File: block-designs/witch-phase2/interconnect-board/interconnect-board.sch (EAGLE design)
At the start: 10 parts

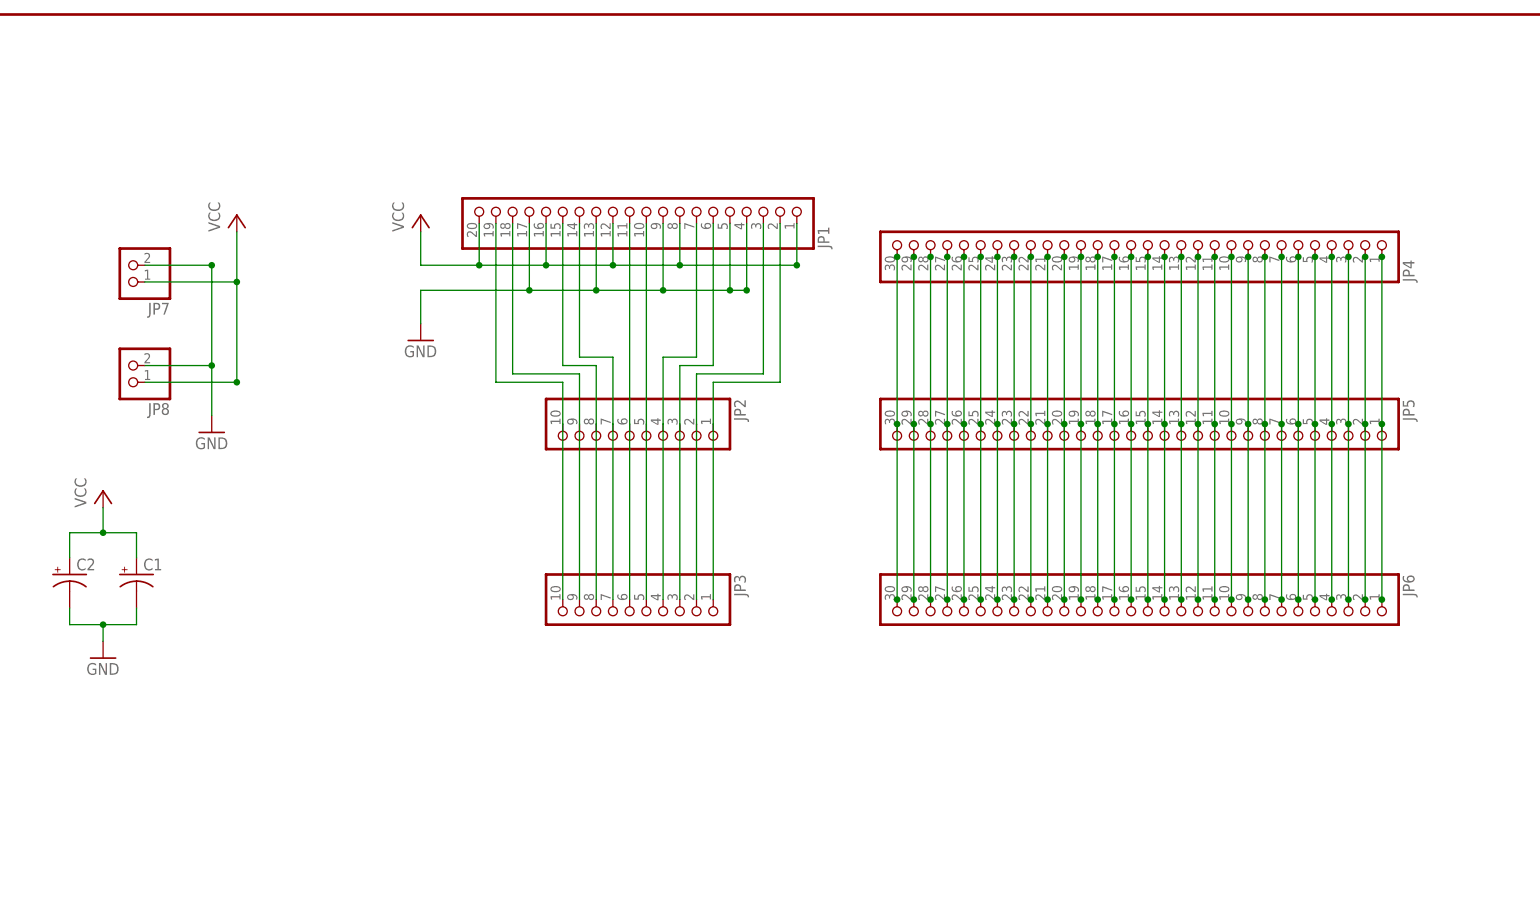
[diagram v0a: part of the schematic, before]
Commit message: update the interconnect board with spacing and layout changes
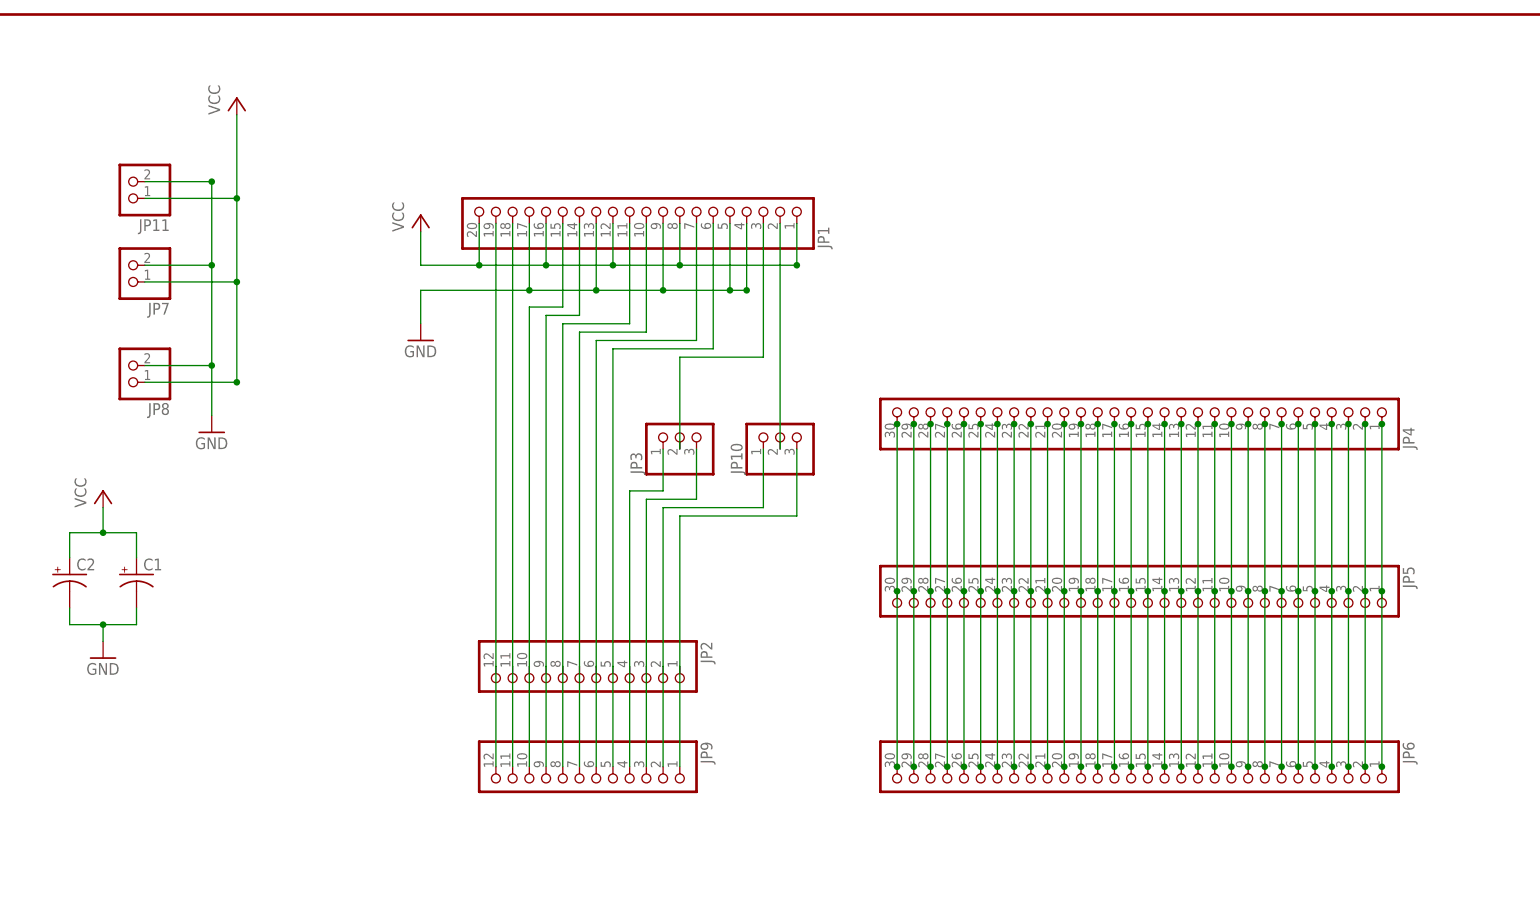
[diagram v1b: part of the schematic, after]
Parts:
- added JP10: (no value), pinhead:PINHD-1X3
- added JP11: (no value), pinhead:PINHD-1X2
- added JP9: (no value), pinhead:PINHD-1X12
- JP2: device pinhead:PINHD-1X10 -> pinhead:PINHD-1X12
- JP3: device pinhead:PINHD-1X10 -> pinhead:PINHD-1X3
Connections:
- new net N$41: JP10.1, JP2.2, JP9.2
- new net N$43: JP1.3, JP3.2
- new net N$44: JP1.2, JP10.2
- new net N$46: JP10.3, JP2.1, JP9.1
- net GND: now also JP11.2
- net N$31: now also JP2.12, JP9.12; no longer JP2.10, JP3.10
- net N$32: now also JP2.11, JP9.11; no longer JP2.9, JP3.9
- net N$33: now also JP2.10, JP9.10; no longer JP2.8, JP3.8
- net N$34: now also JP2.9, JP9.9; no longer JP2.7, JP3.7
- net N$35: now also JP2.8, JP9.8; no longer JP2.6, JP3.6
- net N$36: now also JP2.7, JP9.7; no longer JP2.5, JP3.5
- net N$37: now also JP2.6, JP9.6; no longer JP2.4, JP3.4
- net N$38: now also JP2.5, JP9.5; no longer JP2.3, JP3.3
- net N$39: now also JP2.4, JP3.1, JP9.4; no longer JP1.3, JP2.2, JP3.2
- net N$40: now also JP2.3, JP3.3, JP9.3; no longer JP1.2, JP2.1, JP3.1
- net VCC: now also JP11.1
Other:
- moved on the sheet: JP4, JP5, JP6

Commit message: updated design for layout for use with dupont connectors
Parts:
- added JP12: (no value), pinhead:PINHD-1X2
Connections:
- net GND: now also JP12.2
- net VCC: now also JP12.1
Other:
- moved on the sheet: C1, C2
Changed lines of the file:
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@@
 <part name="JP10" library="pinhead" deviceset="PINHD-1X3" device=""/>
 <part name="JP11" library="pinhead" deviceset="PINHD-1X2" device=""/>
+<part name="JP12" library="pinhead" deviceset="PINHD-1X2" device=""/>
 </parts>
 <sheets>
@@
 <instance part="P+5" gate="VCC" x="88.9" y="236.22"/>
 <instance part="P+1" gate="VCC" x="60.96" y="254"/>
-<instance part="GND2" gate="1" x="57.15" y="203.2"/>
-<instance part="C1" gate="G$1" x="45.72" y="181.61"/>
-<instance part="C2" gate="G$1" x="35.56" y="181.61"/>
-<instance part="GND3" gate="1" x="40.64" y="168.91"/>
-<instance part="P+2" gate="VCC" x="40.64" y="194.31"/>
+<instance part="GND2" gate="1" x="57.15" y="176.53"/>
+<instance part="C1" gate="G$1" x="57.15" y="135.89"/>
+<instance part="C2" gate="G$1" x="46.99" y="135.89"/>
+<instance part="GND3" gate="1" x="52.07" y="123.19"/>
+<instance part="P+2" gate="VCC" x="52.07" y="148.59"/>
 <instance part="JP9" gate="G$1" x="115.57" y="149.86" rot="R270"/>
 <instance part="JP3" gate="A" x="128.27" y="203.2" rot="R90"/>
 <instance part="JP10" gate="A" x="143.51" y="203.2" rot="R90"/>
 <instance part="JP11" gate="G$1" x="44.45" y="241.3" rot="R180"/>
+<instance part="JP12" gate="G$1" x="44.45" y="195.58" rot="R180"/>
 </instances>
 <busses>
@@
 <wire x1="46.99" y1="238.76" x2="60.96" y2="238.76" width="0.1524" layer="91"/>
 <junction x="60.96" y="238.76"/>
+<pinref part="JP12" gate="G$1" pin="1"/>
+<wire x1="46.99" y1="193.04" x2="60.96" y2="193.04" width="0.1524" layer="91"/>
+<wire x1="60.96" y1="193.04" x2="60.96" y2="210.82" width="0.1524" layer="91"/>
+<junction x="60.96" y="193.04"/>
 </segment>
 <segment>
 <pinref part="C2" gate="G$1" pin="+"/>
-<wire x1="35.56" y1="184.15" x2="35.56" y2="187.96" width="0.1524" layer="91"/>
-<wire x1="35.56" y1="187.96" x2="40.64" y2="187.96" width="0.1524" layer="91"/>
+<wire x1="46.99" y1="138.43" x2="46.99" y2="142.24" width="0.1524" layer="91"/>
+<wire x1="46.99" y1="142.24" x2="52.07" y2="142.24" width="0.1524" layer="91"/>
 <pinref part="P+2" gate="VCC" pin="VCC"/>
-<wire x1="40.64" y1="187.96" x2="40.64" y2="191.77" width="0.1524" layer="91"/>
+<wire x1="52.07" y1="142.24" x2="52.07" y2="146.05" width="0.1524" layer="91"/>
 <pinref part="C1" gate="G$1" pin="+"/>
-<wire x1="45.72" y1="184.15" x2="45.72" y2="187.96" width="0.1524" layer="91"/>
-<wire x1="45.72" y1="187.96" x2="40.64" y2="187.96" width="0.1524" layer="91"/>
-<junction x="40.64" y="187.96"/>
+<wire x1="57.15" y1="138.43" x2="57.15" y2="142.24" width="0.1524" layer="91"/>
+<wire x1="57.15" y1="142.24" x2="52.07" y2="142.24" width="0.1524" layer="91"/>
+<junction x="52.07" y="142.24"/>
 </segment>
 </net>
@@
 <wire x1="57.15" y1="228.6" x2="57.15" y2="213.36" width="0.1524" layer="91"/>
 <pinref part="JP8" gate="G$1" pin="2"/>
-<wire x1="57.15" y1="213.36" x2="57.15" y2="205.74" width="0.1524" layer="91"/>
+<wire x1="57.15" y1="213.36" x2="57.15" y2="195.58" width="0.1524" layer="91"/>
+<wire x1="57.15" y1="195.58" x2="57.15" y2="179.07" width="0.1524" layer="91"/>
 <wire x1="46.99" y1="213.36" x2="57.15" y2="213.36" width="0.1524" layer="91"/>
 <junction x="57.15" y="228.6"/>
@@
 <wire x1="57.15" y1="241.3" x2="57.15" y2="228.6" width="0.1524" layer="91"/>
 <junction x="57.15" y="241.3"/>
+<pinref part="JP12" gate="G$1" pin="2"/>
+<wire x1="46.99" y1="195.58" x2="57.15" y2="195.58" width="0.1524" layer="91"/>
+<junction x="57.15" y="195.58"/>
 </segment>
 <segment>
 <pinref part="C2" gate="G$1" pin="-"/>
-<wire x1="35.56" y1="176.53" x2="35.56" y2="173.99" width="0.1524" layer="91"/>
+<wire x1="46.99" y1="130.81" x2="46.99" y2="128.27" width="0.1524" layer="91"/>
 <pinref part="C1" gate="G$1" pin="-"/>
-<wire x1="35.56" y1="173.99" x2="40.64" y2="173.99" width="0.1524" layer="91"/>
-<wire x1="40.64" y1="173.99" x2="45.72" y2="173.99" width="0.1524" layer="91"/>
-<wire x1="45.72" y1="173.99" x2="45.72" y2="176.53" width="0.1524" layer="91"/>
+<wire x1="46.99" y1="128.27" x2="52.07" y2="128.27" width="0.1524" layer="91"/>
+<wire x1="52.07" y1="128.27" x2="57.15" y2="128.27" width="0.1524" layer="91"/>
+<wire x1="57.15" y1="128.27" x2="57.15" y2="130.81" width="0.1524" layer="91"/>
 <pinref part="GND3" gate="1" pin="GND"/>
-<wire x1="40.64" y1="171.45" x2="40.64" y2="173.99" width="0.1524" layer="91"/>
-<junction x="40.64" y="173.99"/>
-</segment>
-</net>
+<wire x1="52.07" y1="125.73" x2="52.07" y2="128.27" width="0.1524" layer="91"/>
+<junction x="52.07" y="128.27"/>
+</segment>
+</net>
